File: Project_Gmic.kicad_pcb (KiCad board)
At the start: 2 copper layers, 40 parts, among them J1 SecondaryBoard_L, J2 SecondaryBoard_R, SW1 SW_SPST, U1 ADA4807-1, U2 ADA4807-4, U3 ADA4807-1, U4 XC6351A120MR-G

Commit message: Searching for parts
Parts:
- added C20: 100nF, Capacitor_SMD:C_0805_2012Metric, F.Cu at (161.7, 90.0)
- added L1: BLM21PG331SN1D, Inductor_SMD:L_0805_2012Metric, F.Cu at (139.1, 86.6)
- added L2: BLM21PG331SN1D, Inductor_SMD:L_0805_2012Metric, F.Cu at (143.7, 86.6)
- added R13: 80k, Resistor_SMD:R_0805_2012Metric, F.Cu at (170.9, 90.2)
- added R14: 100k, Resistor_SMD:R_0805_2012Metric, F.Cu at (175.7, 85.8)
- added R15: 100k, Resistor_SMD:R_0805_2012Metric, F.Cu at (159.6, 102.0)
- added RV1: P160KN-0QC15C500K, Potentiometer_THT:Potentiometer_Alps_RK09K_Single_Horizontal, F.Cu at (124.5, 83.0)
- C1: value 100nF -> 2.2uF
- C10, C12, C16: value 10uF -> 1uF
- C13, C14, C18: value 1uF -> 100nF; footprint Capacitor_SMD:CP_Elec_4x4.5 -> Capacitor_SMD:C_0805_2012Metric
- C15: value 100nF -> 1uF; footprint Capacitor_SMD:C_0805_2012Metric -> Capacitor_SMD:CP_Elec_4x4.5
- C19, C8: value 10uF -> 100nF; footprint Capacitor_SMD:CP_Elec_4x4.5 -> Capacitor_SMD:C_0805_2012Metric
- C2: value 100pF -> 2.2uF
- C4, C9: value 100nF -> 100pF
- C5: value 100pF -> 100nF
- C6: value 10uF -> 100pF; footprint Capacitor_SMD:CP_Elec_4x4.5 -> Capacitor_SMD:C_0805_2012Metric
- J1: value SecondaryBoard_L -> USB4085-GF-A; footprint Connector_PinHeader_2.54mm:PinHeader_1x03_P2.54mm_Horizontal -> Connector_USB:USB_C_Receptacle_GCT_USB4085
- J2: value SecondaryBoard_R -> SJ1-3523N; footprint Connector_PinHeader_2.54mm:PinHeader_1x03_P2.54mm_Horizontal -> SJ13523N:SJ13523N
- MK1: value Microphone1 -> CMC-9745-44P; footprint Battery:BatteryHolder_Keystone_104_1x23mm -> CMC974544P:CMC974544P
- MK2: value Microphone2 -> CMC-9745-44P; footprint Battery:BatteryHolder_Keystone_104_1x23mm -> CMC974544P:CMC974544P
- R1, R2: value 200k -> 2k2
- R10: value 100k -> 80k
- R11, R12: value 10k -> 80k
- R3: value 100k -> 5.1k
- R4: value 80k -> 5.1k
- R6: value 10k -> 2.2k
- R7: value 80k -> 2.2k
- SW1: value SW_SPST -> SW_SPDT; footprint Button_Switch_SMD:SW_DIP_SPSTx01_Slide_9.78x4.72mm_W8.61mm_P2.54mm -> Button_Switch_SMD:SW_SPDT_PCM12
- U1: value ADA4807-1 -> MCP6479; footprint Package_TO_SOT_SMD:SOT-23-6_Handsoldering -> Package_SO:SOIC-14_3.9x8.7mm_P1.27mm
- U2: value ADA4807-4 -> MCP6476U; footprint Package_SO:SOIC-14_3.9x8.7mm_P1.27mm -> Package_TO_SOT_SMD:SOT-23-5
- U3: value ADA4807-1 -> MCP6476U; footprint Package_TO_SOT_SMD:SOT-23-6_Handsoldering -> Package_TO_SOT_SMD:SOT-23-5
- moved C13 58.2 mm to (171.2, 87.2)
- moved U2 58.0 mm to (120.7, 105.5)
- moved J1 54.7 mm to (152.5, 74.1)
- moved SW1 52.3 mm to (154.6, 86.7)
- moved C16 51.6 mm to (138.7, 104.4)
- moved U1 50.0 mm to (165.5, 77.6)
- moved C10 47.7 mm to (173.6, 75.4)
- moved C3 45.6 mm to (176.4, 79.8)
- moved MK1 44.3 mm to (145.3, 77.6)
- moved C6 41.0 mm to (130.6, 104.8)
- moved C8 37.9 mm to (166.2, 90.0)
- moved C14 35.3 mm to (171.2, 84.2)
- moved C4 34.4 mm to (175.7, 82.8)
- moved R1 34.2 mm to (155.1, 103.9)
- moved C19 30.2 mm to (171.9, 79.8)
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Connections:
- C1 pad 1: Net-(C1-Pad1) -> /AUDIO_1_IN
- C1 pad 2: /Uout_highFilter -> Net-(C1-Pad2)
- C10 pad 2: GND -> GNDA
- C11 pad 1: GND -> GNDA
- C12 pad 1: GND -> GNDA
- C13 pad 1: Net-(C13-Pad1) -> +5V
- C13 pad 2: Net-(C13-Pad2) -> GNDA
- C14 pad 2: GND -> GNDA
- C15 pad 1: +5V -> Net-(C15-Pad1)
- C15 pad 2: GND -> Net-(C15-Pad2)
- C17 pad 1: GND -> +5V
- C17 pad 2: -5V -> GNDA
- C18 pad 1: GND -> GNDA
- C19 pad 1: GND -> GNDA
- C2 pad 1: GND -> /AUDIO_2_IN
- C3 pad 1: +5V -> Net-(C3-Pad1)
- C3 pad 2: GND -> /AUDIO_PASS_LOW
- C4 pad 1: Net-(C4-Pad1) -> GNDA
- C5 pad 1: GND -> Net-(C5-Pad1)
- C6 pad 1: +5V -> /AUDIO_PASS_LOW
- C6 pad 2: GND -> Net-(C6-Pad2)
- C7 pad 1: GND -> +5V
- C7 pad 2: -5V -> GNDA
- C8 pad 1: GND -> Net-(C8-Pad1)
- C8 pad 2: -5V -> Net-(C5-Pad1)
- C9 pad 1: +5V -> GNDA
- C9 pad 2: GND -> Net-(C9-Pad2)
- J2 pad 1: GND -> GNDA
- J2 pad 2: /R_POT_OUT -> Net-(J2-Pad2)
- J2 pad 3: GND -> Net-(J2-Pad3)
- MK1 pad 1: Net-(MK1-Pad1) -> GNDA
- MK1 pad 2: +5V -> Net-(C1-Pad2)
- MK2 pad 1: Net-(MK2-Pad1) -> GNDA
- MK2 pad 2: +5V -> Net-(C2-Pad2)
- R1 pad 1: Net-(R1-Pad1) -> +5V
- R1 pad 2: Net-(MK2-Pad1) -> Net-(C1-Pad2)
- R10 pad 1: /R_POT_IN -> Net-(C6-Pad2)
- R11 pad 1: /~DISABLE -> /AUDIO_PASS_HIGH
- R11 pad 2: +5V -> Net-(C5-Pad1)
- R12 pad 1: GND -> Net-(C9-Pad2)
- R12 pad 2: /R_POT_OUT -> Net-(C6-Pad2)
- R2 pad 1: Net-(R1-Pad1) -> +5V
- R2 pad 2: Net-(MK1-Pad1) -> Net-(C2-Pad2)
- R3 pad 1: /Uout_average -> Net-(J1-PadB5)
- R3 pad 2: Net-(R1-Pad1) -> GND
- R4 pad 1: Net-(C2-Pad2) -> Net-(J1-PadA5)
- R4 pad 2: /Uout_average -> GND
- R5 pad 1: GND -> Net-(C4-Pad2)
- R5 pad 2: Net-(C1-Pad1) -> /AUDIO_AVERAGE
- R6 pad 1: GND -> Net-(R6-Pad1)
- R6 pad 2: /Uout_average -> /AUDIO_1_IN
- R7 pad 1: Net-(C5-Pad2) -> Net-(R6-Pad1)
- R7 pad 2: Net-(R7-Pad2) -> /AUDIO_2_IN
- R8 pad 1: GND -> GNDA
- R8 pad 2: Net-(C4-Pad1) -> Net-(C3-Pad1)
- R9 pad 1: Net-(R10-Pad2) -> /AUDIO_AVERAGE
- R9 pad 2: /Uout_lowFilter -> Net-(R6-Pad1)
- SW1 pad 1: /~DISABLE -> /AUDIO_OUT
- SW1 pad 2: GND -> Net-(J2-Pad2)
- U1 pad 1: /Uout_average -> Net-(R10-Pad2)
- U1 pad 2: -5V -> Net-(R10-Pad2)
- U1 pad 3: GND -> Net-(C4-Pad2)
- U1 pad 4: Net-(R1-Pad1) -> +5V
- U1 pad 5: /~DISABLE -> Net-(C3-Pad1)
- U1 pad 6: +5V -> Net-(C5-Pad2)
- U2 pad 1: Net-(C4-Pad2) -> GNDA
- U2 pad 2: Net-(C4-Pad2) -> -5V
- U2 pad 3: Net-(C1-Pad1) -> Net-(R6-Pad1)
- U2 pad 4: +5V -> /AUDIO_AVERAGE
- U2 pad 5: Net-(C4-Pad1) -> +5V
- U3 pad 1: /R_POT_OUT -> GNDA
- U3 pad 3: GND -> Net-(R14-Pad1)
- U3 pad 4: Net-(R10-Pad2) -> /AUDIO_OUT
- U3 pad 5: /~DISABLE -> +5V
- U4 pad 3: Net-(C13-Pad1) -> Net-(C15-Pad1)
- U4 pad 6: Net-(C13-Pad2) -> Net-(C15-Pad2)

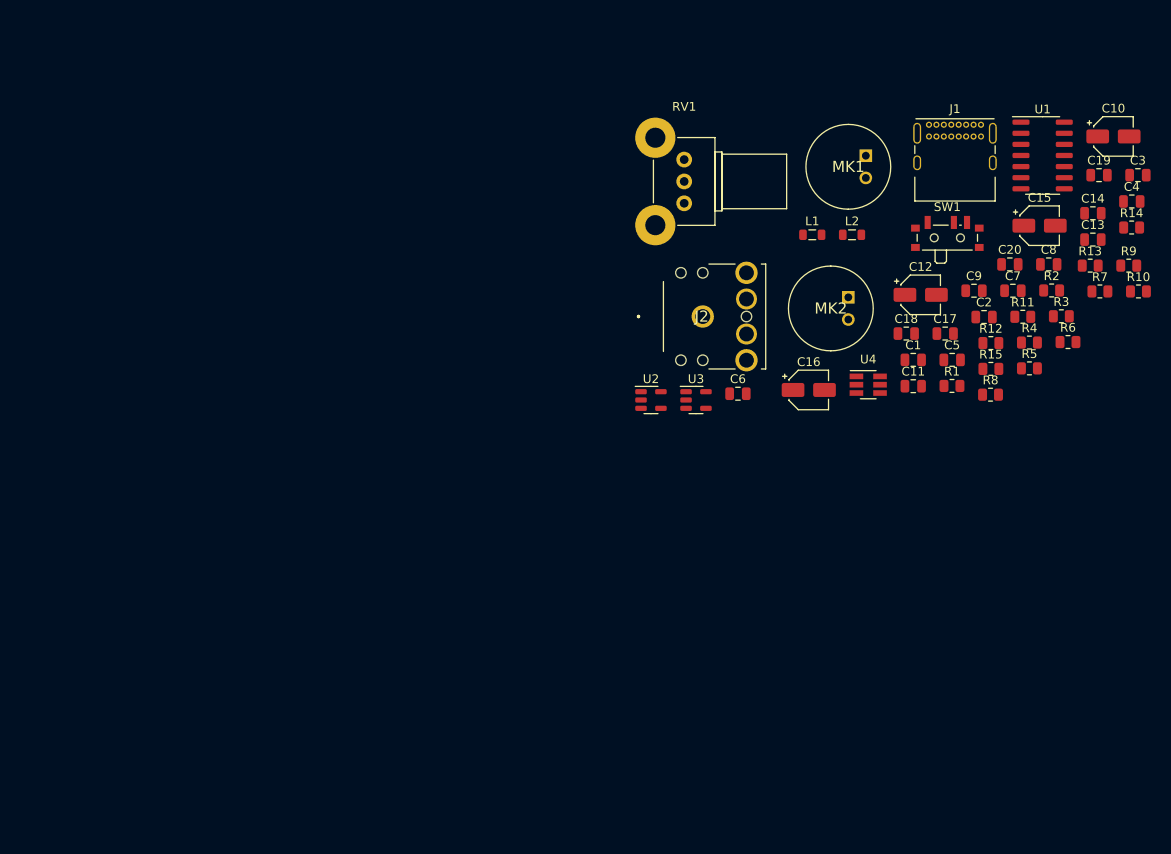
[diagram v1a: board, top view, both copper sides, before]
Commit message: First iteration of the PCB, Rpot
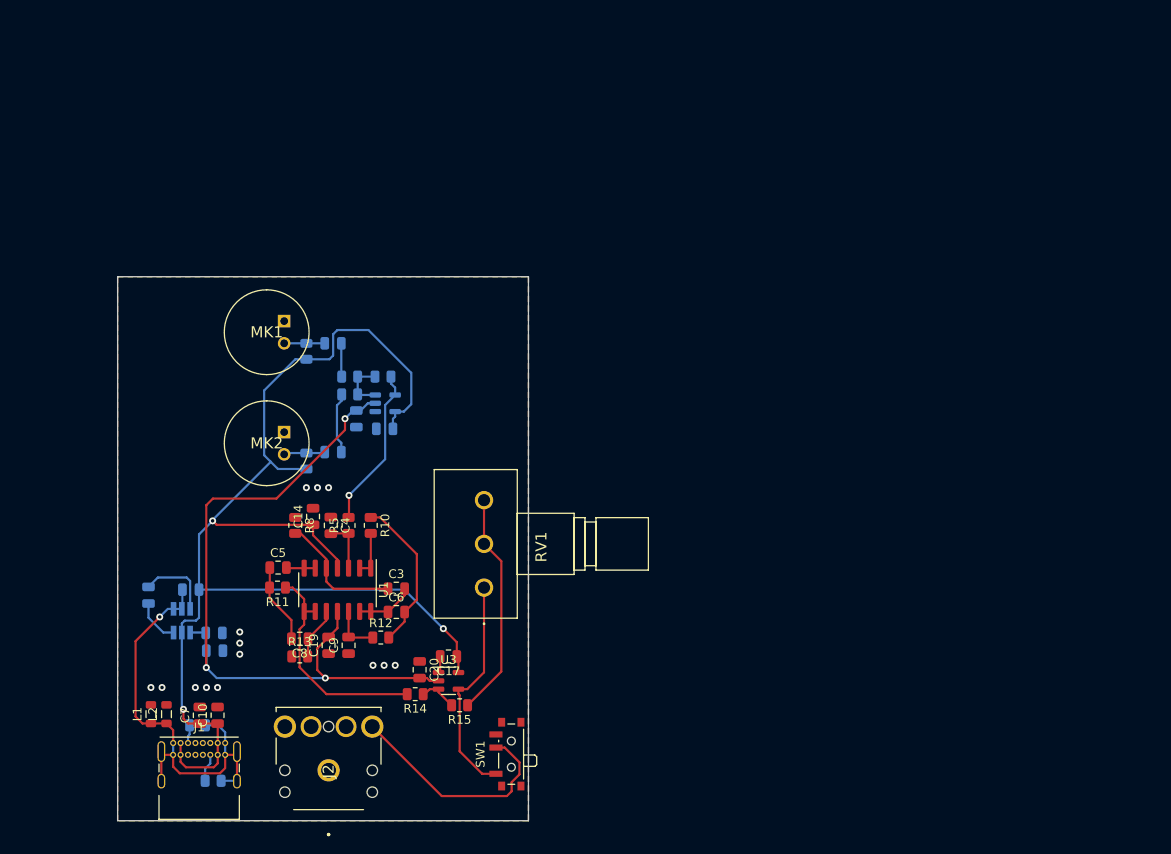
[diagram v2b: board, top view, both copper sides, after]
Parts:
- C1, C11, C13, C18, C2, R1, R2, R3, R4, R6, R7, R9, U2, U4: moved to B.Cu
- C10: footprint Capacitor_SMD:CP_Elec_4x4.5 -> Capacitor_SMD:C_0805_2012Metric
- C12, C15, C16: footprint Capacitor_SMD:CP_Elec_4x4.5 -> Capacitor_SMD:C_0805_2012Metric; moved to B.Cu
- RV1: footprint Potentiometer_THT:Potentiometer_Alps_RK09K_Single_Horizontal -> P160KN0QC15C250K:P160KN0QC15C250K
- moved C10 122.0 mm to (71.1, 141.6), turned to 90 degrees
- moved J1 111.7 mm to (66.0, 144.8)
- moved R3 110.6 mm to (70.6, 149.1)
- moved C15 110.3 mm to (63.2, 127.9), turned to 270 degrees
- moved C7 104.9 mm to (69.1, 141.6), turned to 90 degrees
- moved R4 104.7 mm to (68.8, 142.7)
- moved C19 103.2 mm to (83.8, 133.6), turned to 90 degrees
- moved R13 100.9 mm to (80.5, 134.9)
- moved C4 98.8 mm to (84.1, 119.9), turned to 270 degrees
- moved R14 97.8 mm to (93.7, 139.2), turned to 180 degrees
- moved C3 97.1 mm to (91.6, 127.1)
- moved C8 95.8 mm to (80.5, 132.8), turned to 180 degrees
- moved C14 95.7 mm to (82.0, 118.9), turned to 90 degrees
- moved L2 95.7 mm to (65.3, 141.5), turned to 90 degrees
- moved U1 94.7 mm to (84.8, 127.3), turned to 270 degrees
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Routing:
- net +5V: track 0.00 -> 147.2 mm, vias 0 -> 3
- net -5V: track 0.00 -> 85.4 mm, vias 0 -> 3
- net GND: track 0.00 -> 51.6 mm, vias 0 -> 1
- net Net-(J2-Pad2): track 0.00 -> 26.5 mm
- net Net-(R15-Pad1): track 0.00 -> 25.9 mm
- net /AUDIO_OUT: track 0.00 -> 25.8 mm
- net /AUDIO_PASS_HIGH: track 0.00 -> 25.6 mm
- net /AUDIO_AVERAGE: track 0.00 -> 18.5 mm, vias 0 -> 1
- net Net-(C6-Pad2): track 0.00 -> 17.9 mm
- net Net-(C3-Pad1): track 0.00 -> 14.7 mm
- net Net-(C5-Pad1): track 0.00 -> 9.18 mm
- net Net-(C15-Pad1): track 0.00 -> 8.56 mm
- net /AUDIO_2_IN: track 0.00 -> 7.03 mm
- net /AUDIO_PASS_LOW: track 0.00 -> 6.72 mm
- net Net-(R6-Pad1): track 0.00 -> 6.06 mm
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- added copper zone on B.Cu, net GNDA
- added copper zone on F.Cu, net GNDA
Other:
- board outline added: 47 x 62.2 mm

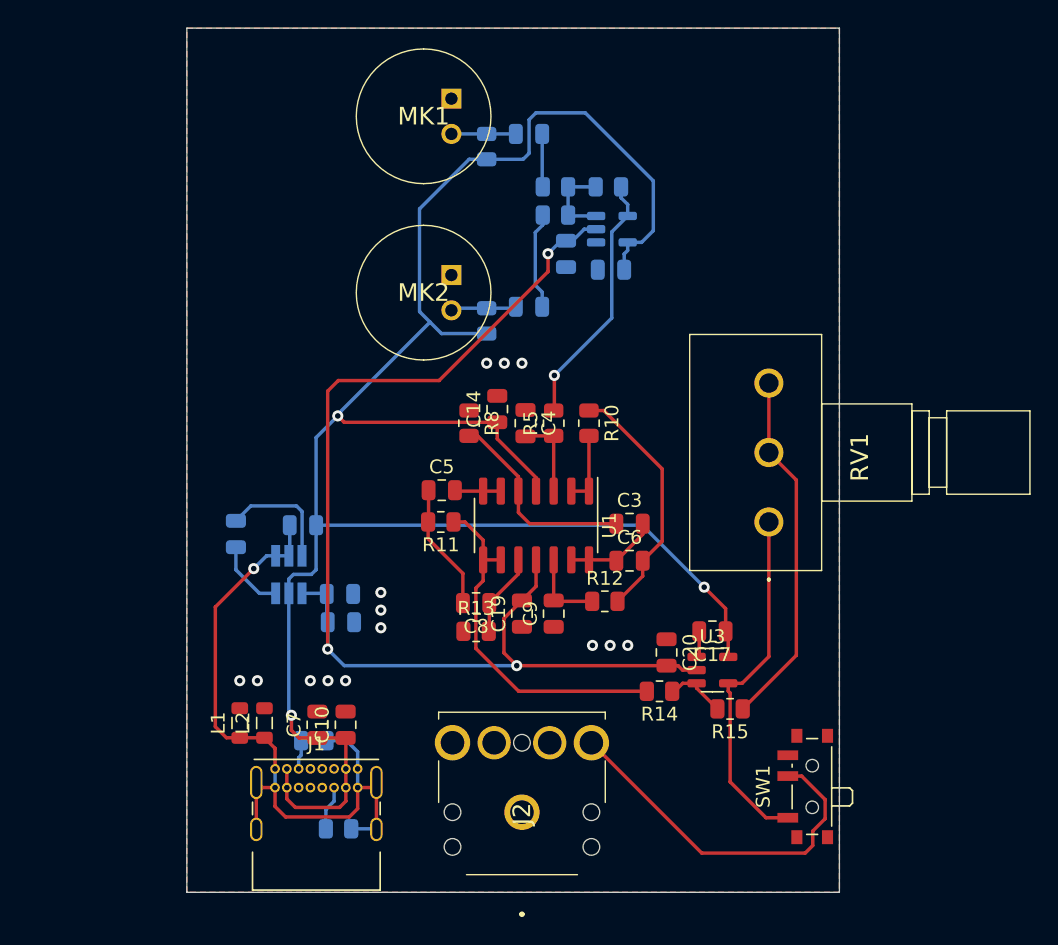
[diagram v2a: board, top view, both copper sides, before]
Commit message: Changing the potentiometer, finishing placement and board
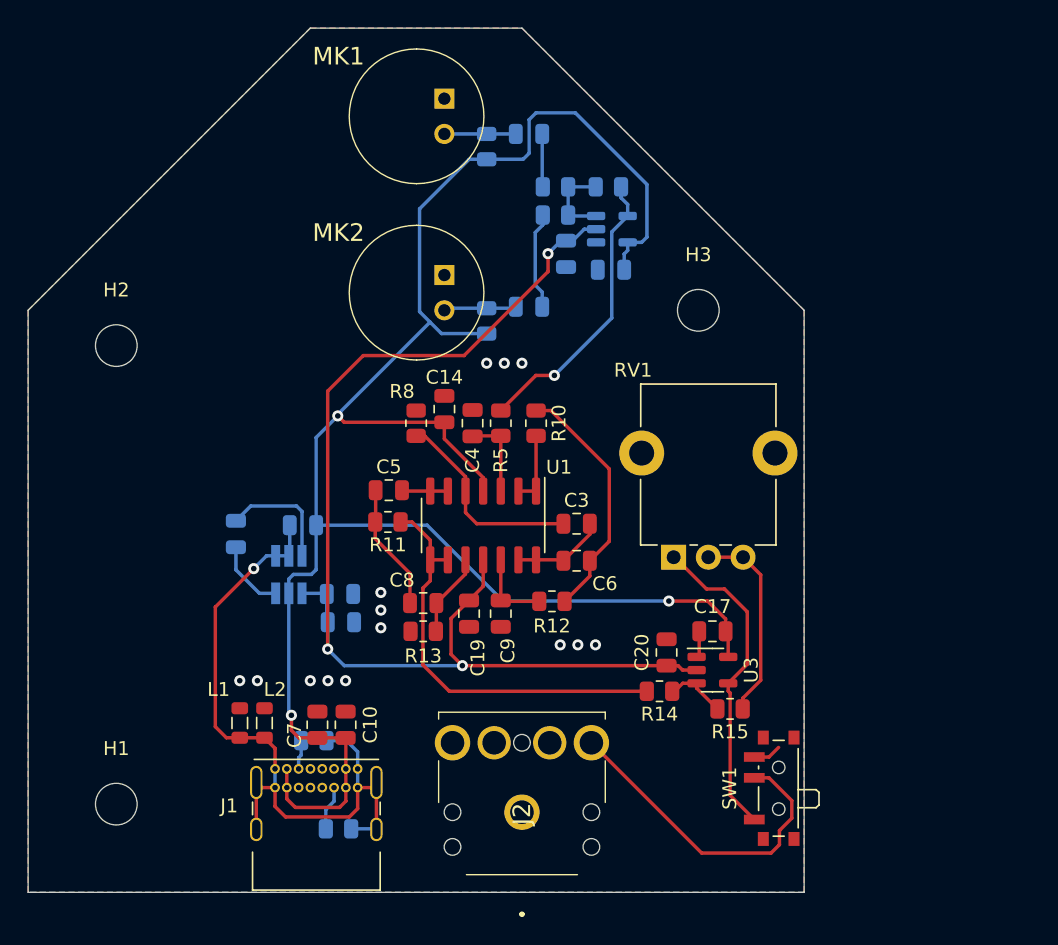
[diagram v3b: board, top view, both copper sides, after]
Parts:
- added H1: MountingHole_3mm, MountingHole:MountingHole_3mm, F.Cu at (54.6, 147.3)
- added H2: MountingHole_3mm, MountingHole:MountingHole_3mm, F.Cu at (54.6, 114.3)
- added H3: MountingHole_3mm, MountingHole:MountingHole_3mm, F.Cu at (96.5, 111.8)
- R15: value 100k -> 80k
- RV1: value P160KN-0QC15C500K -> PTV09A-5025F-A503; footprint P160KN0QC15C250K:P160KN0QC15C250K -> Potentiometer_THT:Potentiometer_Alpha_RD901F-40-00D_Single_Vertical_CircularHoles
- moved RV1 7.31 mm to (94.7, 129.5)
- moved C14 3.81 mm to (78.2, 118.9)
- moved C4 3.81 mm to (80.3, 119.9)
- moved C5 3.81 mm to (74.2, 124.7)
- moved C8 3.81 mm to (76.7, 132.8)
- moved R10 3.81 mm to (84.8, 119.9)
- moved R12 3.81 mm to (86.0, 132.7)
- moved R13 3.81 mm to (76.7, 134.9)
- moved R8 3.81 mm to (76.2, 119.9)
- moved U1 3.81 mm to (81.0, 127.3)
- moved C19 3.81 mm to (80.0, 133.6)
- moved C3 3.81 mm to (87.8, 127.1)
- moved C6 3.81 mm to (87.8, 129.8)
- moved C9 3.81 mm to (82.3, 133.6)
- moved R11 3.81 mm to (74.2, 127.0)
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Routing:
- net Net-(R15-Pad1): track 25.9 -> 14.5 mm
- net +5V: track 147.2 -> 142.1 mm
- net /AUDIO_PASS_HIGH: track 25.6 -> 30.1 mm
- net /AUDIO_OUT: track 25.8 -> 23.2 mm
- net Net-(J2-Pad2): track 26.5 -> 24.0 mm
- net /AUDIO_AVERAGE: track 18.5 -> 20.9 mm
- net GNDA: track 1.92 -> 3.96 mm
- net Net-(C2-Pad2): track 4.74 -> 5.46 mm
- net Net-(C1-Pad2): track 4.64 -> 5.15 mm
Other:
- board size 47 x 62.2 mm -> 55.9 x 62.2 mm
